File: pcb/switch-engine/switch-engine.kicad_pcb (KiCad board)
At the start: 10 copper layers, 124 x 111 mm, 368 parts, among them J1 CONN_PCIE_PWR_8PIN, J10 CORTEX_DEBUG_ETM, J11 SMPM, J12 CONN_01X03, J13 PMOD_HOST, J14 ARF6-08-S-D-A-K-TR, J15 ARF6-08-S-D-A-K-TR, J16 CONN_01X10, J17 ARF6-08-S-D-A-K-TR, J18 ARF6-08-S-D-A-K-TR, J19 CONN_01X10, J2 CONN_IBC_MGMT, J20 0826-1G1T-23-F, J21 ARF6-08-S-D-A-K-TR, J22 ARF6-08-S-D-A-K-TR, J23 CONN_01X10, J24 SMPM, J26 RJ45, J3 CONN_01X03, J4 CORTEX_DEBUG_ETM, J5 FAN_01, J6 FAN_01, J7 JUMPER_0402, J8 XILINX_JTAG, J9 PMOD_HOST, M1 SCREWHOLE, M2 SCREWHOLE, M3 SCREWHOLE, M4 SCREWHOLE, M5 LOGO, M6 LOGO, M7 LOGO, M8 960-27-23-D-AB-0, Q2 SSM6N58NU, SW1 SWITCH, SW2 SWITCH, U1 STM32L431-QFN48, U10 74LVC1T45, U11 74LVC1T45, U12 74LVC1T45, U13 MT25QU256ABA8E12-0AUT, U14 ECS-1612MV-250-CN, U15 SIT9121AI-2BF-XXS156.250000G, U17 AT24MAC402, U18 74LVC1T45, U19 74LVC1T45, U2 MYMGK1R812ERSR, U20 74LVC1T45, U21 74LVC1T45, U22 ECS-1612MV-250-CN, U23 KSZ9031RN, U24 ESD224DQAR, U25 SIT9121AI-2BF-XXS156.250000G, U26 ESD224DQAR, U27 SIT9121AI-2BF-XXS156.250000G, U28 ADP1740ACPZ-2.5-R7, U29 ADM3101E_QFN, U3 MYMGK1R812ERSR, U4 MYMGK00506ERSR, U5 MYMGK00504ERSR, U6 MYMGK00504ERSR, U7 ADP1740ACPZ-1.8-R7, U8 XCKU5P-2FFVB676I, U9 STM32H735-UFBGA176-25

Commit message: Initial floorplanning of northwest area
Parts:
- R70: moved to B.Cu
- moved J1 50.0 mm to (51.0, 64.0)
- moved R70 32.7 mm to (55.5, 105.0), turned to 180 degrees
- moved C149 32.6 mm to (69.5, 59.5)
- moved R71 32.6 mm to (65.5, 59.5)
- moved R9 32.6 mm to (69.5, 63.0)
- moved C150 17.1 mm to (64.9, 52.0)
- moved C151 17.1 mm to (64.4, 55.0)
- moved U29 17.1 mm to (68.9, 53.5)
- moved C152 17.1 mm to (60.9, 52.0)
- moved C153 17.1 mm to (60.4, 55.0)
- moved C112 16.9 mm to (23.5, 69.5)
- moved C113 16.9 mm to (12.8, 67.0)
- moved C114 16.9 mm to (5.25, 62.5)
- moved C115 16.9 mm to (0.75, 68.2)
- moved C116 16.9 mm to (4.75, 68.2)
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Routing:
- net /GND: track 1153.5 -> 1180.1 mm, vias 483 -> 484
- net /MCU/FPGA_PMOD_DQ4: track 10.0 -> 33.9 mm
- net /MCU/FMC_A22: track 8.91 -> 30.2 mm, vias 1 -> 2
- net /MCU/FPGA_PMOD_DQ5: track 10.3 -> 31.3 mm
- net /MCU/FPGA_PMOD_DQ6: track 9.37 -> 30.2 mm
- net /MCU/FPGA_PMOD_DQ1: track 10.9 -> 31.7 mm
- net /MCU/FPGA_PMOD_DQ0: track 9.65 -> 30.1 mm
- net /MCU/FPGA_PMOD_DQ7: track 8.97 -> 29.0 mm
- net /MCU/MCU_UART_TX: track 0.00 -> 19.4 mm, vias 0 -> 1
- net /MCU/FMC_A21: track 9.54 -> 28.9 mm, vias 1 -> 2
- net /MCU/MCU_UART_RX: track 0.00 -> 19.3 mm, vias 0 -> 1
- net /3V3: track 312.3 -> 331.1 mm
- net /MCU/FPGA_PMOD_DQ2: track 8.77 -> 26.5 mm
- net /MCU/MCU_RST_N: track 0.00 -> 17.7 mm, vias 0 -> 2
- net /MCU/FPGA_PMOD_DQ3: track 11.0 -> 28.5 mm
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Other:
- board text added: "FPGA PMOD"
- board text added: "MCU DEBUG"

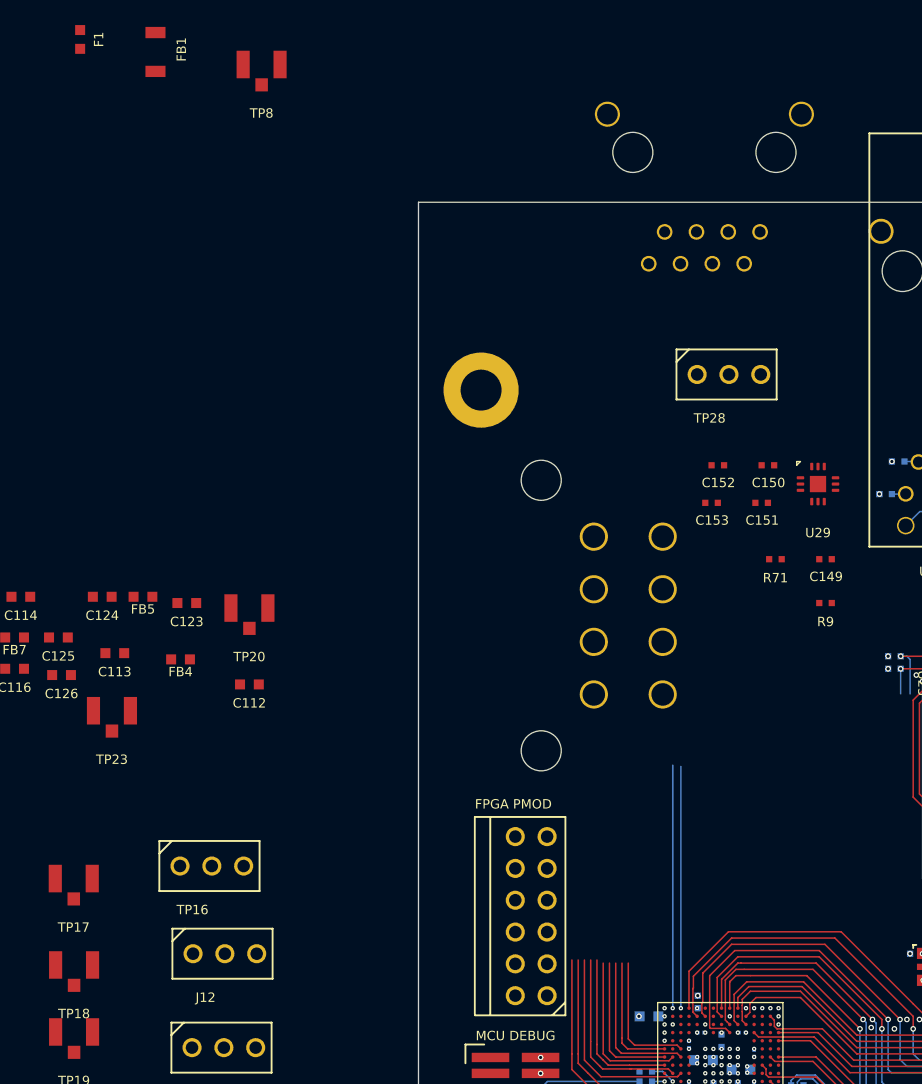
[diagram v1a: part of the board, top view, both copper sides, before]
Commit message: More routing in northwest area
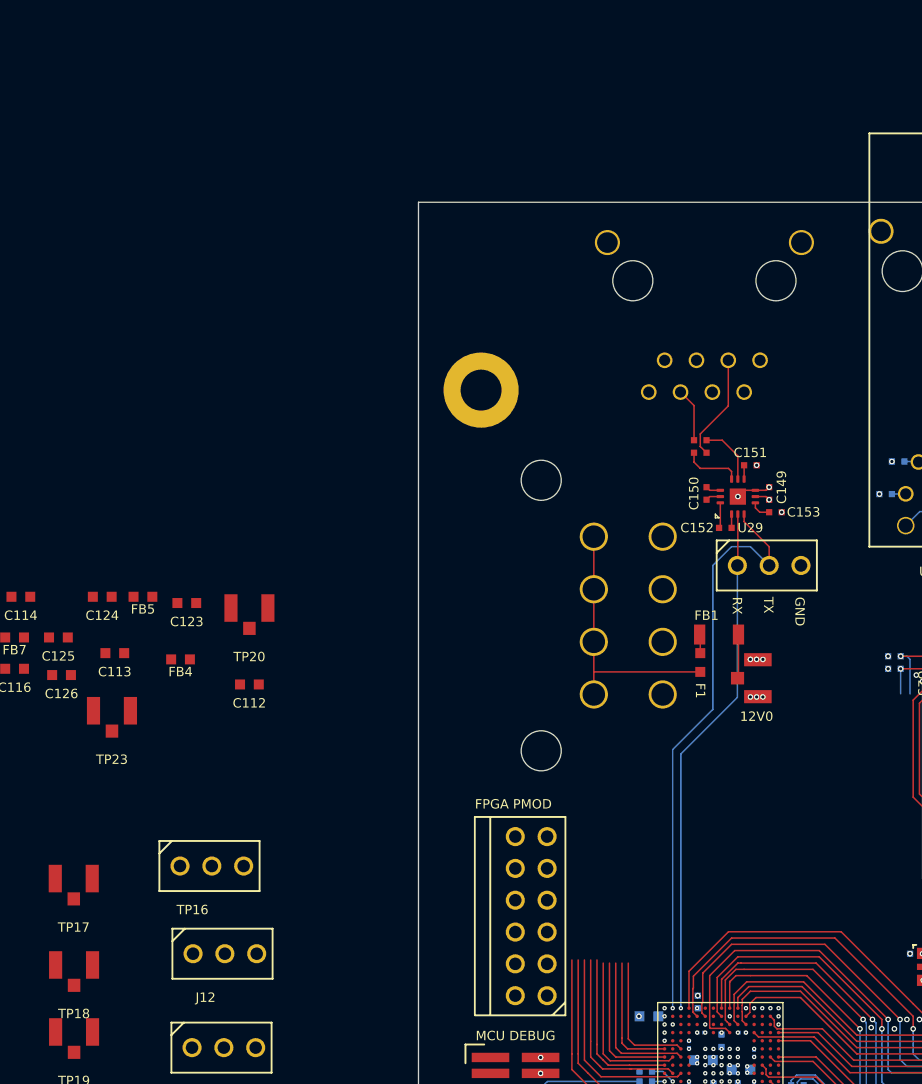
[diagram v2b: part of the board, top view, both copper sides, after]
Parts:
- moved F1 70.2 mm to (59.5, 67.8)
- moved FB1 64.7 mm to (61.0, 65.5), turned to 0 degrees
- moved TP8 62.9 mm to (64.0, 69.0), turned to -90 degrees
- moved R9 15.7 mm to (60.0, 50.5), turned to -90 degrees
- moved TP28 15.6 mm to (65.0, 60.0)
- moved R71 11.1 mm to (59.0, 50.5), turned to 90 degrees
- moved J26 10.2 mm to (65.5, 37.3)
- moved C149 6.91 mm to (65.0, 54.2), turned to 90 degrees
- moved U29 6.48 mm to (62.5, 54.5), turned to 90 degrees
- moved C150 5.39 mm to (60.0, 54.2), turned to 90 degrees
- moved C153 5.15 mm to (65.5, 55.8)
- moved C152 5.04 mm to (61.5, 57.0), turned to 180 degrees
- moved C151 3.13 mm to (63.5, 52.0)
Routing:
- net /GND: track 1180.1 -> 1331.4 mm, vias 484 -> 494
- net /MCU/MCU_UART_TX: track 19.4 -> 47.3 mm
- net /MCU/MCU_UART_RX: track 19.3 -> 41.3 mm
- net Net-(J1-12V0_SENSE): track 0.00 -> 21.3 mm
- net /3V3: track 331.1 -> 347.5 mm, vias 42 -> 43
- net /MCU/RS232_TX_RJ45: track 0.00 -> 8.52 mm
- net /MCU/RS232_TX: track 0.00 -> 4.87 mm
- net /MCU/RS232_RX: track 0.00 -> 4.66 mm
- net /MCU/RS232_RX_RJ45: track 0.00 -> 4.29 mm
- net /Power Supply/12V0: track 32.3 -> 35.8 mm
- net Net-(U29-C1-): track 0.00 -> 2.04 mm
- net Net-(U29-V+): track 0.00 -> 1.64 mm
- net Net-(F1-Pad2): track 0.00 -> 1.51 mm
- net Net-(U29-C2+): track 0.00 -> 1.20 mm
- net Net-(U29-C2-): track 0.00 -> 1.20 mm
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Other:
- board text added: "12V0"
- board text added: "RX"
- board text added: "TX"

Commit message: Continued layout of MCU area, added cutout for fan
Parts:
- added M9: FAN, azonenberg_pcb:FAN_DELTA_EFB0412VHD-SP05, F.Cu at (114.0, 48.0)
- C88, R67, U14: moved to B.Cu
- moved TP10 161.5 mm to (64.0, 74.0), turned to -90 degrees
- moved TP25 159.6 mm to (178.2, 68.8)
- moved TP15 158.6 mm to (64.0, 79.0), turned to -90 degrees
- moved TP13 149.1 mm to (70.0, 69.0), turned to 90 degrees
- moved TP23 57.9 mm to (70.0, 79.0), turned to 90 degrees
- moved TP16 57.1 mm to (67.8, 116.0), turned to 180 degrees
- moved TP19 54.7 mm to (61.2, 115.0), turned to 180 degrees
- moved C5 53.1 mm to (197.8, 27.5)
- moved J2 53.1 mm to (213.0, 25.9)
- moved TP18 52.3 mm to (56.5, 115.0), turned to 180 degrees
- moved TP20 47.7 mm to (70.0, 74.0), turned to 90 degrees
- moved C38 44.3 mm to (147.3, 45.0)
- moved D3 44.3 mm to (143.3, 36.5)
- moved D4 44.3 mm to (140.0, 36.5)
- moved J5 44.3 mm to (144.3, 38.0)
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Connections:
- U8 pad E11: /MCU/FMC_NBL1 -> /MCU/FMC_NWE
- U8 pad E12: /MCU/FMC_NE2 -> /MCU/FMC_A24
- U8 pad E20: /RGMII PHY/ETH_LED2_N_1V8 -> /RGMII PHY/ETH_LED1_N_1V8
- U8 pad F10: /MCU/FMC_A22 -> /MCU/FMC_A23
- U8 pad F12: /MCU/FMC_A19 -> /MCU/FMC_NE2
- U8 pad F9: /MCU/FMC_A20 -> /MCU/FMC_NOE
- U8 pad G10: /MCU/FMC_NBL0 -> /MCU/FMC_NBL1
- U8 pad G11: /MCU/FMC_A23 -> /MCU/FMC_A19
- U8 pad G12: /MCU/FMC_A24 -> /MCU/FMC_A22
- U8 pad G14: /MCU/FMC_AD3 -> /MCU/FMC_A21
- U8 pad G21: /RGMII PHY/ETH_LED1_N_1V8 -> /RGMII PHY/ETH_LED2_N_1V8
- U8 pad G9: /MCU/FMC_A21 -> /MCU/FMC_AD3
- U8 pad H11: /MCU/FPGA_PMOD_DQ2 -> /MCU/FPGA_PMOD_DQ4
- U8 pad H12: /MCU/FPGA_LED_1 -> /MCU/FPGA_PMOD_DQ5
- U8 pad H13: /MCU/FPGA_LED_0 -> /MCU/FPGA_PMOD_DQ6
- U8 pad H14: /MCU/FMC_NWE -> /MCU/FMC_NBL0
- U8 pad H9: /MCU/FPGA_PMOD_DQ7 -> /MCU/FPGA_LED_1
- U8 pad J10: /MCU/FPGA_PMOD_DQ5 -> /MCU/FPGA_LED_0
- U8 pad J11: /MCU/FPGA_PMOD_DQ0 -> /MCU/FPGA_PMOD_DQ1
- U8 pad J12: /MCU/FPGA_LED_2 -> /MCU/FPGA_PMOD_DQ2
- U8 pad J13: /MCU/FPGA_LED_3 -> /MCU/FPGA_PMOD_DQ3
- U8 pad J14: /MCU/FPGA_PMOD_DQ6 -> /MCU/FPGA_PMOD_DQ7
- U8 pad J15: /MCU/FMC_NOE -> /MCU/FMC_A20
- U8 pad J9: /MCU/FPGA_PMOD_DQ4 -> /MCU/FPGA_LED_2
- U8 pad K10: /MCU/FPGA_PMOD_DQ3 -> /MCU/FPGA_PMOD_DQ0
- U8 pad K9: /MCU/FPGA_PMOD_DQ1 -> /MCU/FPGA_LED_3
- U9 pad B8: unconnected-(U9D-PD7-PadB8) -> /MCU/MCU_LED_0
- U9 pad C1: unconnected-(U9C-PC13-PadC1) -> /MCU/MCU_LED_3
- U9 pad C6: unconnected-(U9B-PB5-PadC6) -> /MCU/MCU_LED_2
- U9 pad C8: unconnected-(U9G-PG10-PadC8) -> /MCU/MCU_LED_1
- U9 pad G3: unconnected-(U9F-PF2-PadG3) -> /MCU/MCU_PMOD_DQ3
- U9 pad H2: unconnected-(U9F-PF4-PadH2) -> /MCU/MCU_PMOD_DQ2
- U9 pad J2: unconnected-(U9F-PF8-PadJ2) -> /MCU/MCU_PMOD_DQ6
- U9 pad J3: unconnected-(U9F-PF7-PadJ3) -> /MCU/MCU_PMOD_DQ7
- U9 pad K3: unconnected-(U9F-PF10-PadK3) -> /MCU/MCU_PMOD_DQ1
- U9 pad L15: /MCU/MCU_PMOD_DQ4 -> unconnected-(U9B-PB13-PadL15)
- U9 pad L2: unconnected-(U9C-PC0-PadL2) -> /MCU/MCU_PMOD_DQ5
- U9 pad M1: unconnected-(U9C-PC2-PadM1) -> /MCU/MCU_PMOD_DQ4
- U9 pad M15: /MCU/MCU_PMOD_DQ0 -> unconnected-(U9B-PB12-PadM15)
- U9 pad M2: unconnected-(U9C-PC3-PadM2) -> /MCU/MCU_PMOD_DQ0
- U9 pad N10: /MCU/MCU_LED_2 -> unconnected-(U9F-PF15-PadN10)
- U9 pad N11: /MCU/MCU_LED_1 -> unconnected-(U9F-PF13-PadN11)
- U9 pad N13: /MCU/MCU_LED_0 -> unconnected-(U9H-PH8-PadN13)
- U9 pad N14: /MCU/MCU_PMOD_DQ5 -> unconnected-(U9H-PH10-PadN14)
- U9 pad N15: /MCU/MCU_PMOD_DQ1 -> unconnected-(U9H-PH12-PadN15)
- U9 pad P15: /MCU/MCU_PMOD_DQ6 -> unconnected-(U9H-PH6-PadP15)
- U9 pad P5: /MCU/MCU_PMOD_DQ3 -> unconnected-(U9A-PA4-PadP5)
- U9 pad R10: /MCU/MCU_LED_3 -> unconnected-(U9F-PF14-PadR10)
- U9 pad R4: /MCU/MCU_PMOD_DQ7 -> unconnected-(U9H-PH3-PadR4)
- U9 pad R6: /MCU/MCU_PMOD_DQ2 -> unconnected-(U9C-PC4-PadR6)
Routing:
- net /GND: track 1331.4 -> 1431.1 mm, vias 494 -> 552
- net /3V3: track 347.5 -> 442.4 mm, vias 43 -> 51
- net /GTY_VTT: track 41.5 -> 90.4 mm, vias 15 -> 16
- net /RGMII PHY/ETH_LED1_N_1V8_INV: track 16.6 -> 62.9 mm
- net /MCU/FMC_NE2: track 19.2 -> 63.6 mm, vias 1 -> 2
- net /MCU/FMC_A19: track 23.6 -> 67.7 mm
- net /MCU/FMC_A24: track 22.8 -> 65.0 mm, vias 1 -> 2
- net /MCU/FMC_NBL1: track 20.8 -> 62.8 mm
- net /MCU/FMC_A20: track 24.3 -> 66.0 mm
- net /MCU/MCU_PMOD_DQ4: track 0.00 -> 40.5 mm
- net /1V8: track 126.8 -> 167.1 mm, vias 30 -> 31
- net /MCU/FMC_A23: track 24.4 -> 64.4 mm
- net /MCU/FMC_A25: track 23.2 -> 62.9 mm, vias 1 -> 2
- net /MCU/FMC_NBL0: track 25.8 -> 65.3 mm, vias 1 -> 2
- net /MCU/FMC_NL_NADV: track 22.9 -> 62.3 mm, vias 1 -> 2
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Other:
- board size 124 x 111 mm -> 135 x 111 mm
- board text added: "0-BOOT0-1"
- board text added: "1V8"
- board text added: "A3V3"
- board text added: "D1V2"
- board text added: "GTY_VTT"
- board text added: "MAIN I2C"
- board text added: "SCL"
- board text added: "SDA"
- board text added: "VDDA"
- board text added: "VSMPS"

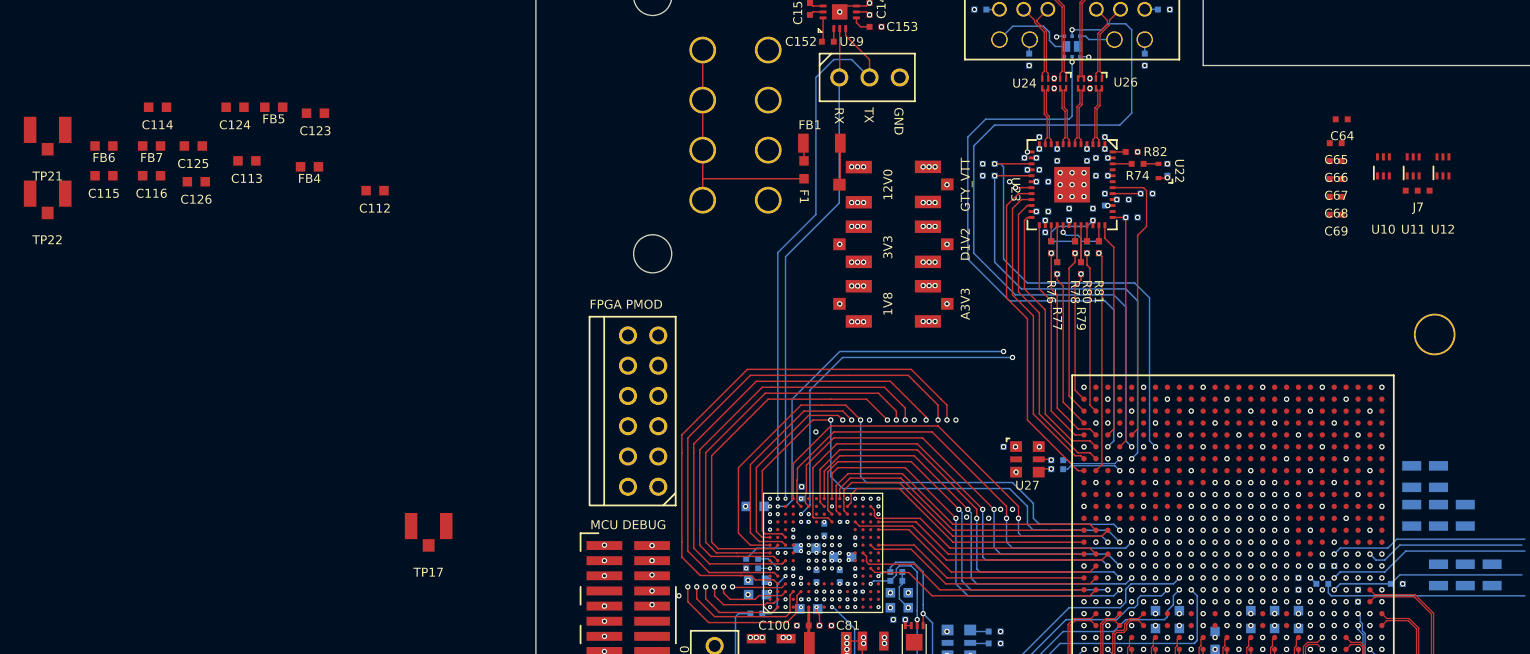
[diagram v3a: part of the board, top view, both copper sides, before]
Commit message: More progress on PHY layout
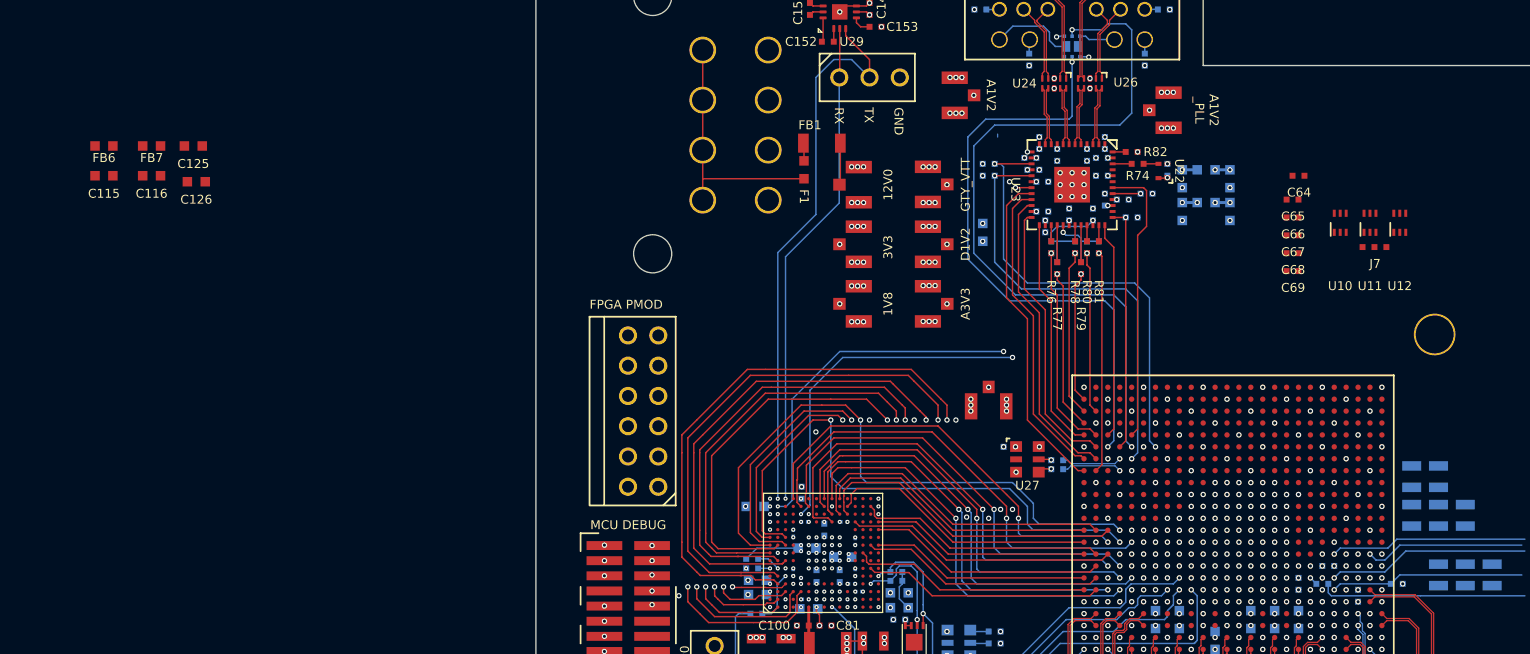
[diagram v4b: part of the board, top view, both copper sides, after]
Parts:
- C112, C113, C114, C123, C124, FB4, FB5: moved to B.Cu
- moved TP21 94.0 mm to (90.0, 62.8), turned to -90 degrees
- moved C113 82.6 mm to (95.2, 71.2), turned to -90 degrees
- moved C124 80.0 mm to (91.2, 71.2), turned to -90 degrees
- moved FB5 78.7 mm to (93.2, 70.5), turned to 180 degrees
- moved TP22 76.7 mm to (72.2, 61.5), turned to 90 degrees
- moved FB4 75.3 mm to (93.2, 67.8), turned to 180 degrees
- moved C123 73.0 mm to (91.2, 68.5), turned to -90 degrees
- moved C112 71.8 mm to (95.2, 68.5), turned to -90 degrees
- moved C114 70.0 mm to (74.5, 73.0), turned to -90 degrees
- moved TP17 48.1 mm to (75.0, 87.5), turned to 180 degrees
- moved U10 5.96 mm to (104.5, 72.2)
- moved U11 5.96 mm to (107.0, 72.2)
- moved U12 5.96 mm to (109.5, 72.2)
- moved C64 5.96 mm to (101.0, 68.2)
- moved C65 5.96 mm to (100.5, 70.2)
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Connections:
- C112 pad 1: /1V2 -> /GTY_VTT
- C115 pad 1: /1V2 -> /GTY_VTT
- FB4 pad 1: /1V2 -> /GTY_VTT
- FB6 pad 1: /1V2 -> /GTY_VTT
- FB7 pad 1: /1V2 -> /GTY_VTT
- U8 pad D13: /MCU/FMC_NL_NADV -> /MCU/FMC_AD2
- U8 pad F13: /MCU/FMC_AD2 -> /MCU/FMC_A25
- U8 pad F14: /MCU/FMC_A25 -> /MCU/FMC_NL_NADV
- U8 pad G12: /MCU/FMC_A22 -> /MCU/FMC_A20
- U8 pad J15: /MCU/FMC_A20 -> /MCU/FMC_A22
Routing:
- net /GND: track 1431.1 -> 1472.5 mm, vias 552 -> 575
- net /MCU/SFP1_SCL: track 34.5 -> 65.0 mm
- net /MCU/SFP1_SDA: track 33.5 -> 63.7 mm
- net /GTY_VTT: track 90.4 -> 118.2 mm, vias 16 -> 18
- net /3V3: track 442.4 -> 459.5 mm, vias 51 -> 53
- net /MCU/VCORE: track 17.5 -> 32.0 mm, vias 3 -> 4
- net /RGMII PHY/A3V3: track 28.0 -> 41.4 mm, vias 4 -> 6
- net /RGMII PHY/A1V2: track 3.30 -> 14.1 mm, vias 2 -> 3
- net /RGMII PHY/D1V2: track 24.6 -> 33.8 mm, vias 7 -> 8
- net /RGMII PHY/A1V2_PLL: track 0.40 -> 7.96 mm, vias 1 -> 2
- net /MCU/FMC_A22: track 67.8 -> 75.1 mm
- net /MCU/FMC_NL_NADV: track 62.3 -> 67.8 mm
- net /MCU/FMC_NBL0: track 65.3 -> 70.6 mm
- net /MCU/FMC_A21: track 68.0 -> 73.0 mm
- net /MCU/FMC_A25: track 62.9 -> 67.8 mm
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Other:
- board text added: "A1V2"
- board text added: "A1V2 _PLL"
